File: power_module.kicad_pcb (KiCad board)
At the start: 4 copper layers, 95 x 76.9 mm, 71 parts, among them J1 USB_C_PD, J2 OUTPUT, J3 I2C_BREAKOUT, Q1 DUAL_N_FET, Q2 DUAL_N_FET, Q3 DUAL_N_FET, Q4 DUAL_N_FET, SW1 ON_OFF, U1 BQ7692003, U2 CH224K, U3 BQ24650, U4 LM5176PWPR

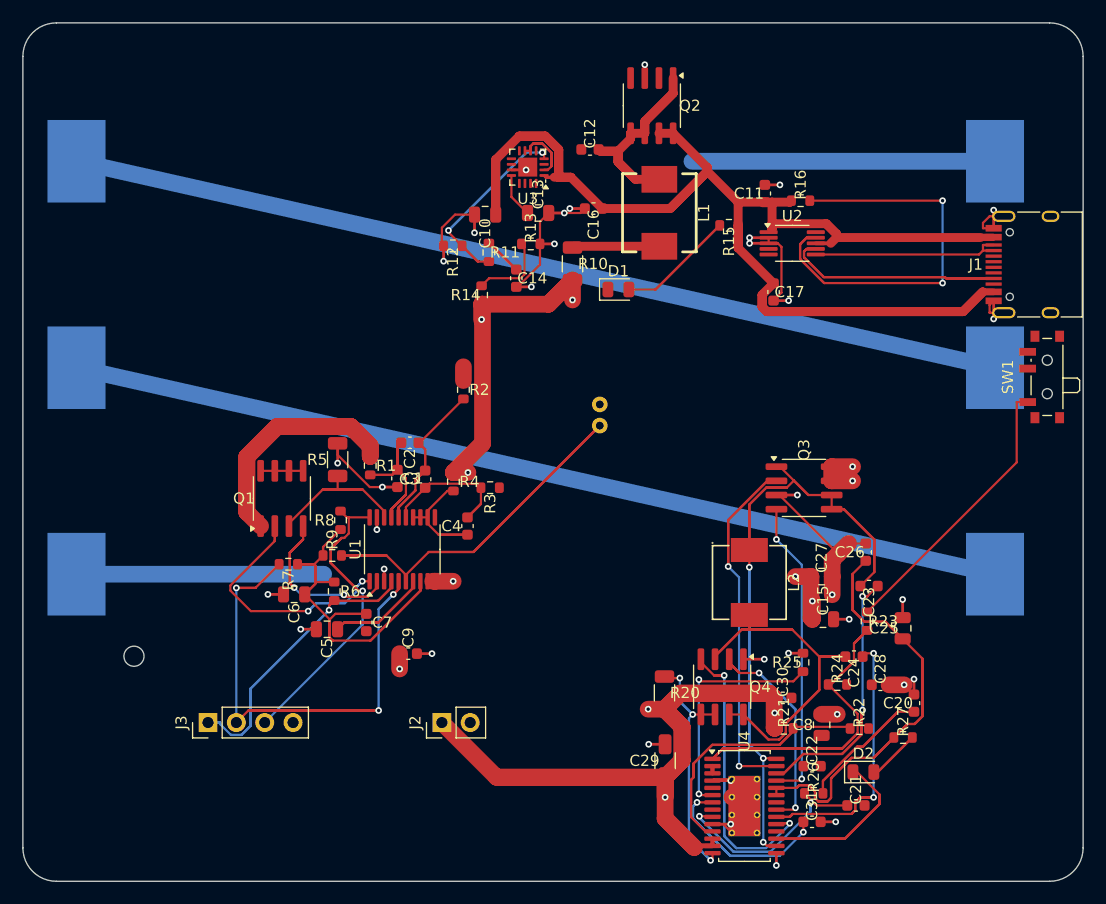
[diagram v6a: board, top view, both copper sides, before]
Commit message: apply pin_zone_same_net v3: 17 paired-pin zones, 7 correctly rejected
After fixing the 2-pad opposite-corner pathology (absoluteMaxDistMm,
#218) and adding foreign-pad-overlap rejection (#219), applied
pin_zone_same_net to the current board. 17 zones placed across
Q1-Q4 dual-FETs, U1/U4 paired pins, J1 shell pads, and the U4
thermal pad on B.Cu.

The 7 rejected zones include exactly the cases the user warned
about: pads at opposite ends of an IC body with foreign-net pads
between them (U2 USB_VBUS 1+8, U3 GND 11+17, U4 F.Cu GND across the
package, J1 USB-C pin pairs with CC/NC pads between).

DRC unchanged at 38 errors. The track_width violations remain
because the original thin pre-route stubs are still on the board
in parallel with the new zones. Deleting those would be a separate
cleanup pass.

Tools touched: develop f5817fc + 9719f28.
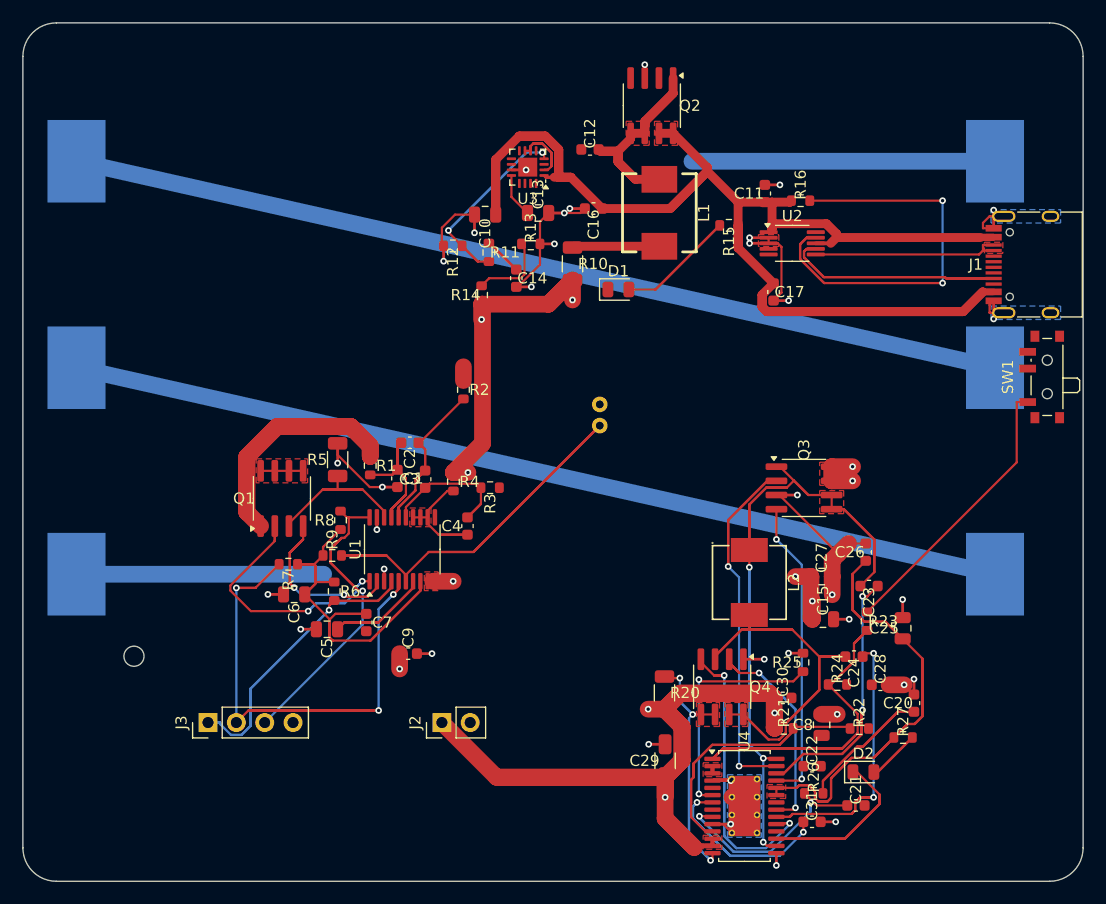
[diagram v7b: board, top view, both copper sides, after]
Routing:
- added copper zone on F.Cu, net BAT+
- added copper zone on F.Cu, net BB_SW1
- added copper zone on F.Cu, net BB_SW2
- added copper zone on F.Cu, net BB_VCC
- added copper zone on F.Cu, net BQ_PH
- added copper zone on F.Cu, net CC2
- added copper zone on F.Cu, net FET_MID
- added copper zone on B.Cu, net GND
- added copper zone on F.Cu, net GND
- added copper zone on F.Cu, net USB_VBUS
- added copper zone on F.Cu, net V12_INT
- added copper zone on F.Cu, net V12_OUT
- added copper zone on F.Cu, net VC3
